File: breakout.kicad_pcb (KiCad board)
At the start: 2 copper layers, 103 x 62 mm, 36 parts, among them CON1 SD_Card, CON2 USB-MICRO-AB, P2 CONN_01X40, P3 CONN_01X40, P4 CONN_01X40, P5 A-DF-09-A/KG-T4S, Q1 SIA461DJ-T1-GE3, Q2 IRLML2402TRPBF, SW1 SW_PUSH

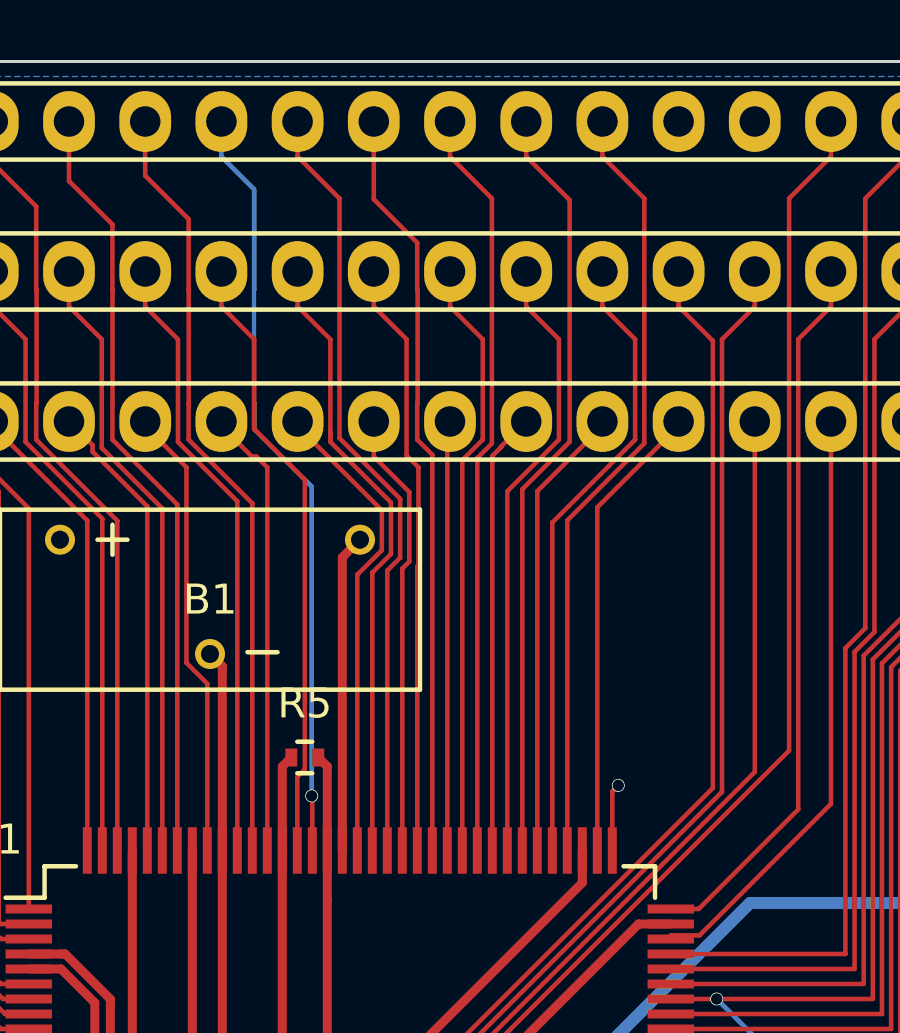
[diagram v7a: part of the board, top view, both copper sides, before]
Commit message: connected RESET to a header pin
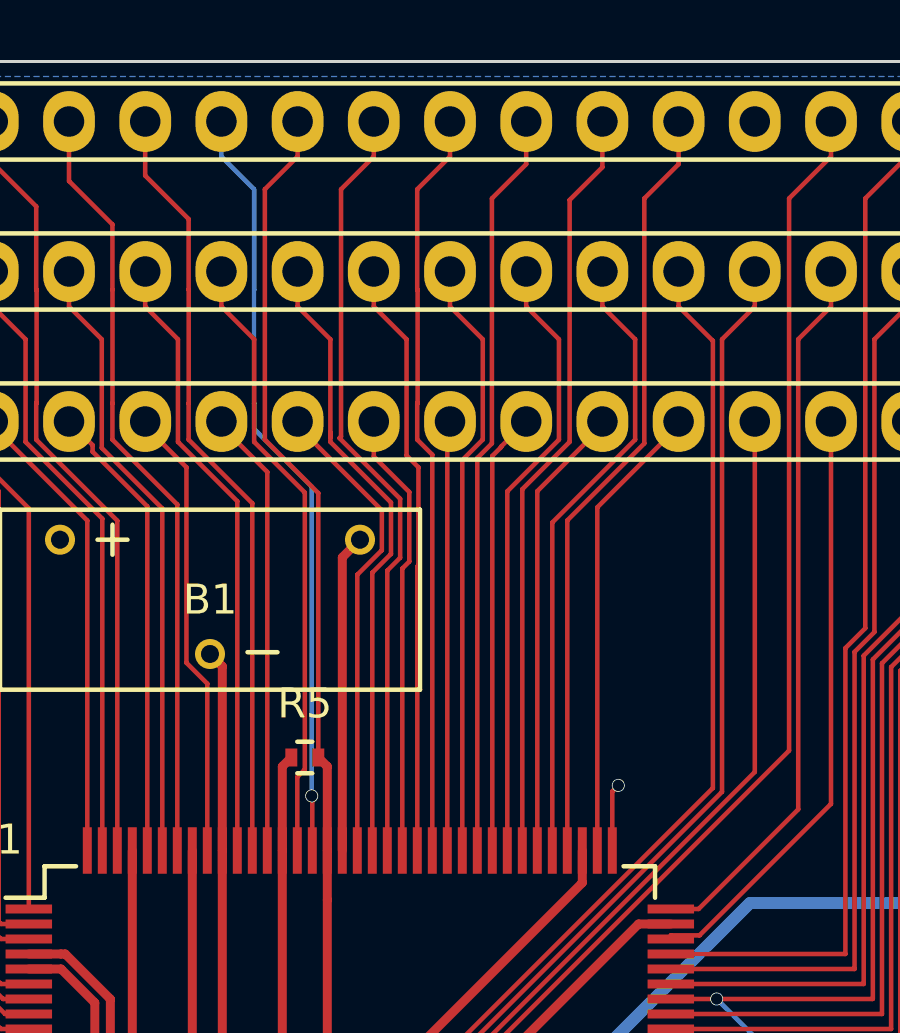
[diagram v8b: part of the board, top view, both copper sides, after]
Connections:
- P2 pad 20: /SPI_SSEL -> /RESET
- P2 pad 21: /P3_5 -> /SPI_SSEL
- P2 pad 22: /SPI_SCK -> /P3_5
- P2 pad 23: /P7_2 -> /SPI_SCK
- P2 pad 24: /P3_0 -> /P7_2
- P2 pad 25: GND -> /P3_0
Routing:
- net /RESET: track 33.7 -> 56.1 mm
